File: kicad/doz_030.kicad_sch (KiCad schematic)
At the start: 28 parts, among them J2 SWD, J3 LCD, J4 RGB, J5 DC-025, J6 Motor, Q1 IRLR2905, SW1 RotaryEncoder_Switch, SW3 MTS-101, U1 LM78M05_TO252, U2 XC6206PxxxMR, U3 STM32F030F4Px, U4 HX

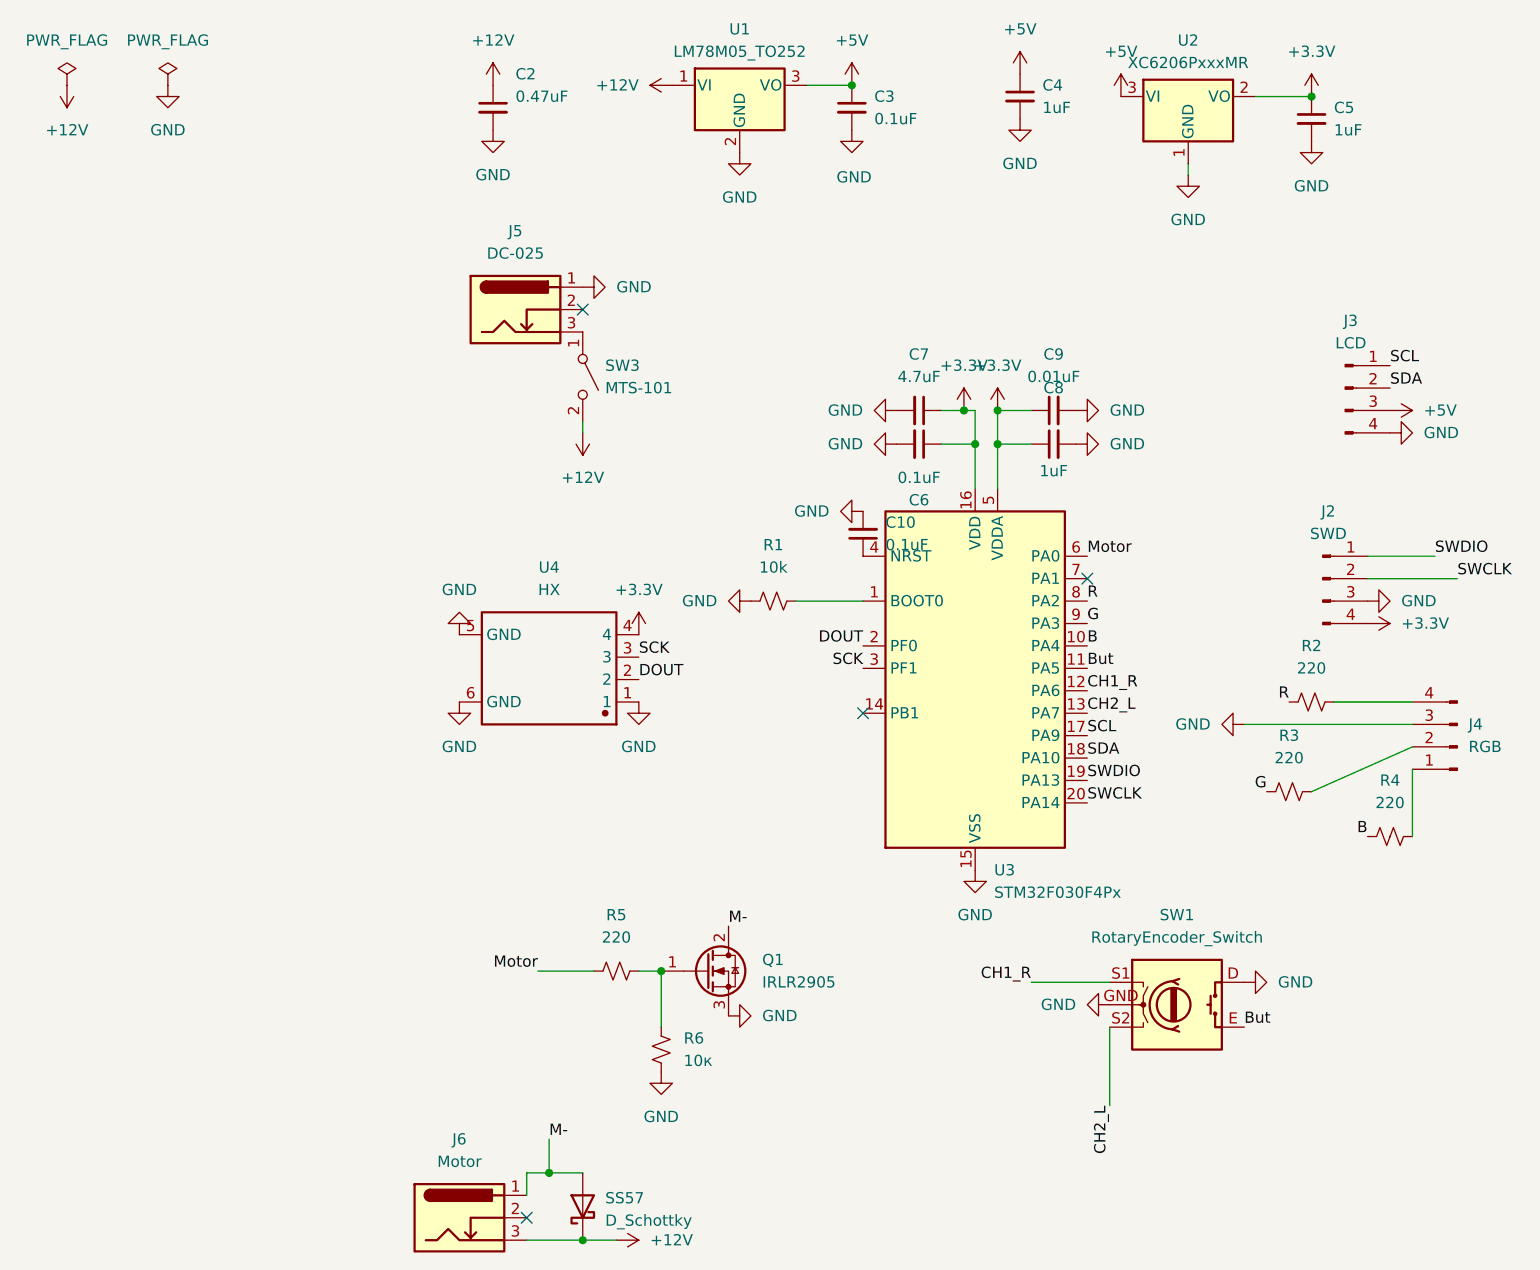
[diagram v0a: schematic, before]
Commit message: Move current KiCad project into firmware repository
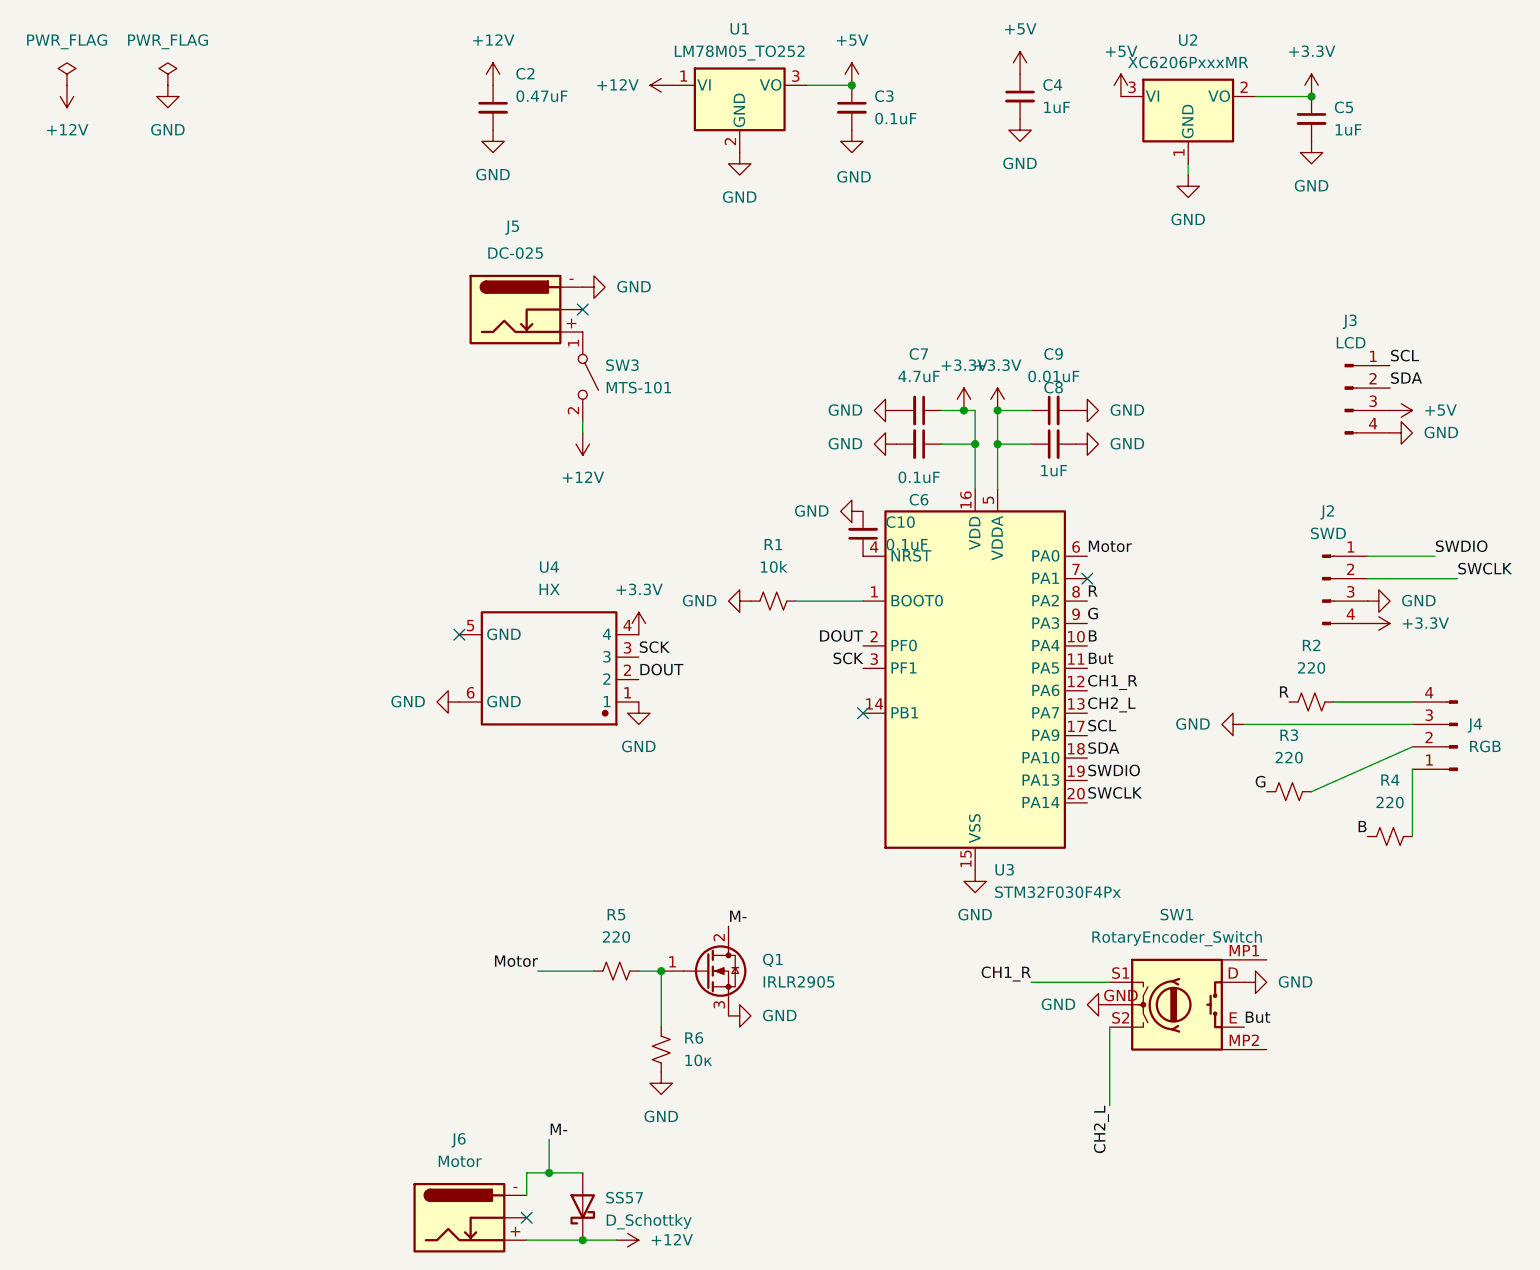
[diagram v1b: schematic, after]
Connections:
- net +12V: now also J6.+ (Sleeve); no longer J6.3 (Sleeve)
- net GND: now also J5.- (Center); no longer J5.1 (Center), U4.5 (GND)
- net M-: now also J6.- (Center); no longer J6.1 (Center)
- net at SW3.1 (A): now also J5.+ (Sleeve); no longer J5.3 (Sleeve)
- no-connect marks 4 -> 5
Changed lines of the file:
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@@
 	)
 	(no_connect
+		(at 63.5 83.82)
+	)
+	(no_connect
 		(at 134.62 77.47)
 	)
@@
 	(symbol
 		(lib_id "power:GND")
+		(at 63.5 91.44 270)
+		(unit 1)
+		(body_style 1)
+		(exclude_from_sim no)
+		(in_bom yes)
+		(on_board yes)
+		(in_pos_files yes)
+		(dnp no)
+		(fields_autoplaced yes)
+		(property "Reference" "#PWR031"
+			(at 57.15 91.44 0)
+			(hide yes)
+			(show_name no)
+			(do_not_autoplace no)
+			(effects
+				(font
+					(size 1.27 1.27)
+				)
+			)
+		)
+		(property "Value" "GND"
+			(at 59.69 91.4399 90)
+			(show_name no)
+			(do_not_autoplace no)
+			(effects
+				(font
+					(size 1.27 1.27)
+				)
+				(justify right)
+			)
+		)
+		(property "Footprint" ""
+			(at 63.5 91.44 0)
+			(hide yes)
+			(show_name no)
+			(do_not_autoplace no)
+			(effects
+				(font
+					(size 1.27 1.27)
+				)
+			)
+		)
+		(property "Datasheet" ""
+			(at 63.5 91.44 0)
+			(hide yes)
+			(show_name no)
+			(do_not_autoplace no)
+			(effects
+				(font
+					(size 1.27 1.27)
+				)
+			)
+		)
+		(property "Description" "Power symbol creates a global label with name \"GND\" , ground"
+			(at 63.5 91.44 0)
+			(hide yes)
+			(show_name no)
+			(do_not_autoplace no)
+			(effects
+				(font
+					(size 1.27 1.27)
+				)
+			)
+		)
+		(pin "1"
+		)
+		(instances
+			(project "doz_030"
+				(path "/b5e4c38e-e014-4885-88d7-17804e8a617c"
+					(reference "#PWR031")
+					(unit 1)
+				)
+			)
+		)
+	)
+	(symbol
+		(lib_id "power:GND")
 		(at 160.02 27.94 0)
 		(unit 1)
@@
 			)
 		)
-		(pin "1"
+		(pin "+"
 		)
-		(pin "3"
+		(pin "~"
 		)
-		(pin "2"
+		(pin "-"
 		)
 		(instances
@@
 	)
 	(symbol
-		(lib_id "power:GND")
-		(at 63.5 83.82 180)
-		(unit 1)
-		(body_style 1)
-		(exclude_from_sim no)
-		(in_bom yes)
-		(on_board yes)
-		(in_pos_files yes)
-		(dnp no)
-		(fields_autoplaced yes)
-		(property "Reference" "#PWR031"
-			(at 63.5 77.47 0)
-			(hide yes)
-			(show_name no)
-			(do_not_autoplace no)
-			(effects
-				(font
-					(size 1.27 1.27)
-				)
-			)
-		)
-		(property "Value" "GND"
-			(at 63.5 78.74 0)
-			(show_name no)
-			(do_not_autoplace no)
-			(effects
-				(font
-					(size 1.27 1.27)
-				)
-			)
-		)
-		(property "Footprint" ""
-			(at 63.5 83.82 0)
-			(hide yes)
-			(show_name no)
-			(do_not_autoplace no)
-			(effects
-				(font
-					(size 1.27 1.27)
-				)
-			)
-		)
-		(property "Datasheet" ""
-			(at 63.5 83.82 0)
-			(hide yes)
-			(show_name no)
-			(do_not_autoplace no)
-			(effects
-				(font
-					(size 1.27 1.27)
-				)
-			)
-		)
-		(property "Description" "Power symbol creates a global label with name \"GND\" , ground"
-			(at 63.5 83.82 0)
-			(hide yes)
-			(show_name no)
-			(do_not_autoplace no)
-			(effects
-				(font
-					(size 1.27 1.27)
-				)
-			)
-		)
-		(pin "1"
-		)
-		(instances
-			(project "doz_030"
-				(path "/b5e4c38e-e014-4885-88d7-17804e8a617c"
-					(reference "#PWR031")
-					(unit 1)
-				)
-			)
-		)
-	)
-	(symbol
 		(lib_id "power:+12V")
 		(at 19.05 21.59 180)
@@
 		(pin "S2"
 		)
+		(pin "MP2"
+		)
+		(pin "MP1"
+		)
 		(instances
 			(project "doz_030"
@@
 		(in_pos_files yes)
 		(dnp no)
-		(fields_autoplaced yes)
 		(property "Reference" "J5"
-			(at 69.85 38.1 0)
+			(at 69.596 37.592 0)
 			(show_name no)
 			(do_not_autoplace no)
@@
 			)
 		)
-		(pin "2"
+		(pin "~"
 		)
-		(pin "1"
+		(pin "-"
 		)
-		(pin "3"
+		(pin "+"
 		)
 		(instances
@@
 					(unit 1)
 				)
-			)
-		)
-	)
-	(symbol
-		(lib_id "power:GND")
-		(at 63.5 91.44 0)
-		(unit 1)
-		(body_style 1)
-		(exclude_from_sim no)
-		(in_bom yes)
-		(on_board yes)
-		(in_pos_files yes)
-		(dnp no)
-		(fields_autoplaced yes)
-		(property "Reference" "#PWR032"
-			(at 63.5 97.79 0)
-			(hide yes)
-			(show_name no)
-			(do_not_autoplace no)
-			(effects
-				(font
-					(size 1.27 1.27)
-				)
-			)
-		)
-		(property "Value" "GND"
-			(at 63.5 96.52 0)
-			(show_name no)
-			(do_not_autoplace no)
-			(effects
-				(font
-					(size 1.27 1.27)
-				)
-			)
-		)
-		(property "Footprint" ""
-			(at 63.5 91.44 0)
-			(hide yes)
-			(show_name no)
-			(do_not_autoplace no)
-			(effects
-				(font
-					(size 1.27 1.27)
-				)
-			)
-		)
-		(property "Datasheet" ""
-			(at 63.5 91.44 0)
-			(hide yes)
-			(show_name no)
-			(do_not_autoplace no)
-			(effects
-				(font
-					(size 1.27 1.27)
-				)
-			)
-		)
-		(property "Description" "Power symbol creates a global label with name \"GND\" , ground"
-			(at 63.5 91.44 0)
-			(hide yes)
-			(show_name no)
-			(do_not_autoplace no)
-			(effects
-				(font
-					(size 1.27 1.27)
-				)
-			)
-		)
-		(pin "1"
-		)
-		(instances
-			(project "doz_030"
-				(path "/b5e4c38e-e014-4885-88d7-17804e8a617c"
-					(reference "#PWR032")
-					(unit 1)
-				)
